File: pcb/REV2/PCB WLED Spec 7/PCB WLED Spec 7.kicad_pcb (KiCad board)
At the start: 2 copper layers, 12 parts, among them J1 USB_C_Receptacle_USB2.0_16P, U1 ESP32-C3, U2 RT9013-33GB, U3 LMR14050SDDAR

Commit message: Update PCB WLED Spec 7.kicad_pcb
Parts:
- added Q1: BC807, Package_TO_SOT_SMD:SOT-23, F.Cu at (163.1, 134.8)
- added Q2: BC807, Package_TO_SOT_SMD:SOT-23, F.Cu at (163.1, 139.5)
- moved D1 19.6 mm to (163.1, 130.2)
- moved U1 17.0 mm to (170.6, 122.0)
- moved U2 8.75 mm to (177.6, 137.6)
- moved C10 3.95 mm to (157.8, 136.2)
- moved C9 3.95 mm to (157.8, 132.8)
- moved J1 3.95 mm to (160.9, 123.2)
- moved C11 3.95 mm to (157.8, 139.5)
- moved C8 3.95 mm to (157.8, 129.5)
- moved S2 3.71 mm to (177.6, 124.4)
- moved S1 3.71 mm to (177.6, 120.3)
- moved U3 1.68 mm to (170.3, 138.5)
- moved D2 1.09 mm to (171.0, 131.2)
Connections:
- net Net-(U1-GPIO2) renamed LED1_IN
- U1 pad 16: unconnected-(U1-GPIO10-Pad16) -> LED2_IN

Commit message: pcb v2 update
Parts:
- removed Q2: BC807, Package_TO_SOT_SMD:SOT-23
- added AE1: 2450AT18A100E, 2450AT18A100E:ANTC3216X140N, F.Cu at (143.8, 96.2)
- added C1: C1µF, Capacitor_SMD:C_0402_1005Metric, F.Cu at (160.9, 95.9)
- added C12: C0.1µF, Capacitor_SMD:C_0402_1005Metric, F.Cu at (197.0, 82.5)
- added C13: C22nF, Capacitor_SMD:C_0402_1005Metric, F.Cu at (199.5, 86.0)
- added C14: C0.1µF, Capacitor_SMD:C_0402_1005Metric, F.Cu at (189.5, 83.0)
- added C15: C4.7µF, Capacitor_SMD:C_0805_2012Metric, F.Cu at (189.0, 86.5)
- added C16: C4.7µF, Capacitor_SMD:C_0805_2012Metric, F.Cu at (189.0, 84.5)
- added C2: C1µF, Capacitor_SMD:C_0402_1005Metric, F.Cu at (160.9, 97.9)
- added C3: C1µF, Capacitor_SMD:C_0402_1005Metric, F.Cu at (160.9, 99.9)
- added C4: C1µF, Capacitor_SMD:C_0402_1005Metric, F.Cu at (163.8, 95.9)
- added C5: C0.1µF, Capacitor_SMD:C_0402_1005Metric, F.Cu at (163.8, 97.9)
- added C6: C10µF, Capacitor_SMD:C_0603_1608Metric, F.Cu at (156.6, 99.0)
- added C7: C0.1µF, Capacitor_SMD:C_0402_1005Metric, F.Cu at (163.8, 99.9)
- added L1: L2nH, Inductor_SMD:L_0603_1608Metric, F.Cu at (156.6, 101.5)
- added L2: L10µH, custom:TECHFUSE SL1050-100M, F.Cu at (204.0, 76.5)
- added R1: R5.1K, Resistor_SMD:R_0402_1005Metric, F.Cu at (188.5, 78.0)
- added R10: R17.8k, Resistor_SMD:R_0402_1005Metric, F.Cu at (197.0, 89.5)
- added R11: R84.5k, Resistor_SMD:R_0402_1005Metric, F.Cu at (192.0, 89.5)
- added R12: R1k, Resistor_SMD:R_0402_1005Metric, F.Cu at (153.2, 88.0)
- added R13: R1k, Resistor_SMD:R_0402_1005Metric, F.Cu at (153.2, 90.0)
- added R2: R5.1K, Resistor_SMD:R_0402_1005Metric, F.Cu at (188.0, 82.0)
- added R3: R22, Resistor_SMD:R_0402_1005Metric_Pad0.72x0.64mm_HandSolder, F.Cu at (189.0, 79.5)
- added R4: R22, Resistor_SMD:R_0402_1005Metric_Pad0.72x0.64mm_HandSolder, F.Cu at (189.0, 80.5)
- added R5: R10k, Resistor_SMD:R_0402_1005Metric, F.Cu at (150.2, 86.0)
- added R6: R10k, Resistor_SMD:R_0402_1005Metric, F.Cu at (150.2, 88.0)
- added R7: R10k, Resistor_SMD:R_0402_1005Metric, F.Cu at (150.2, 90.0)
- added R8: R10k, Resistor_SMD:R_0402_1005Metric, F.Cu at (150.2, 92.0)
- added R9: R100k, Resistor_SMD:R_0402_1005Metric, F.Cu at (199.5, 88.5)
- added S3: solder pad, custom:solder pad small, F.Cu at (189.5, 89.0)
- added S4: solder pad, custom:solder pad small, F.Cu at (187.5, 89.0)
- added S5: solder pad, custom:solder pad small, F.Cu at (186.0, 71.0)
- added S6: solder pad, custom:solder pad small, F.Cu at (186.0, 73.0)
- added S7: solder pad, custom:solder pad small, F.Cu at (183.5, 71.0)
- added S8: solder pad, custom:solder pad small, F.Cu at (183.5, 73.0)
- moved C11 73.9 mm to (189.0, 72.5), turned to -90 degrees
- moved C10 72.0 mm to (191.5, 72.5), turned to -90 degrees
- moved C9 70.4 mm to (194.0, 72.5), turned to -90 degrees
- moved C8 68.9 mm to (196.5, 72.5), turned to -90 degrees
- moved U2 63.2 mm to (195.7, 77.1)
- moved D1 60.4 mm to (191.6, 77.0)
- moved U3 58.0 mm to (194.8, 86.0)
- moved D2 56.1 mm to (205.0, 86.5)
- moved J1 48.7 mm to (182.9, 79.8), turned to -90 degrees
- moved S2 47.4 mm to (195.5, 80.5)
- moved U1 40.9 mm to (144.0, 90.8)
- moved Q1 39.8 mm to (157.1, 95.5)
- moved S1 32.8 mm to (183.0, 88.0)
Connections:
- U1 pad 16: LED2_IN -> LED1_IN
- U1 pad 6: LED1_IN -> PWM1
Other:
- board outline added: 30 x 20 mm

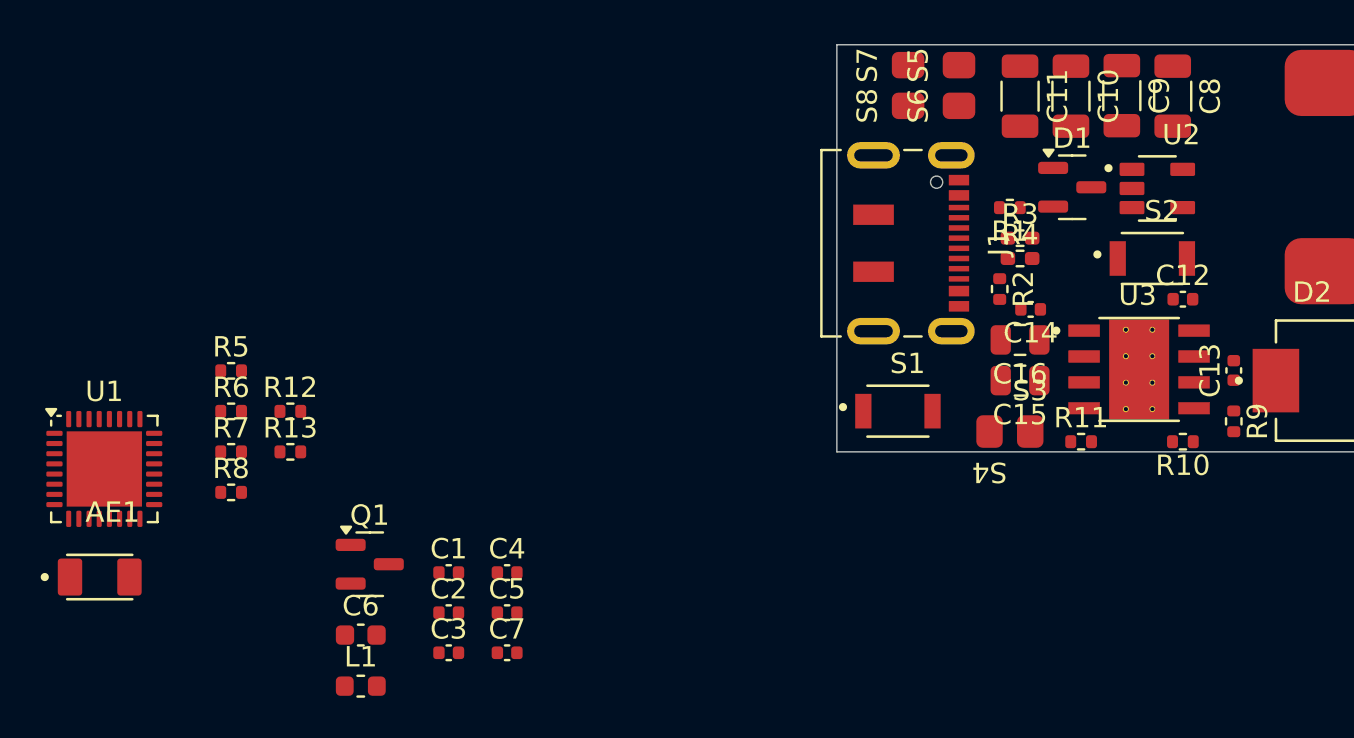
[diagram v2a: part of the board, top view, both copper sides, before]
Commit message: pcb layout finished
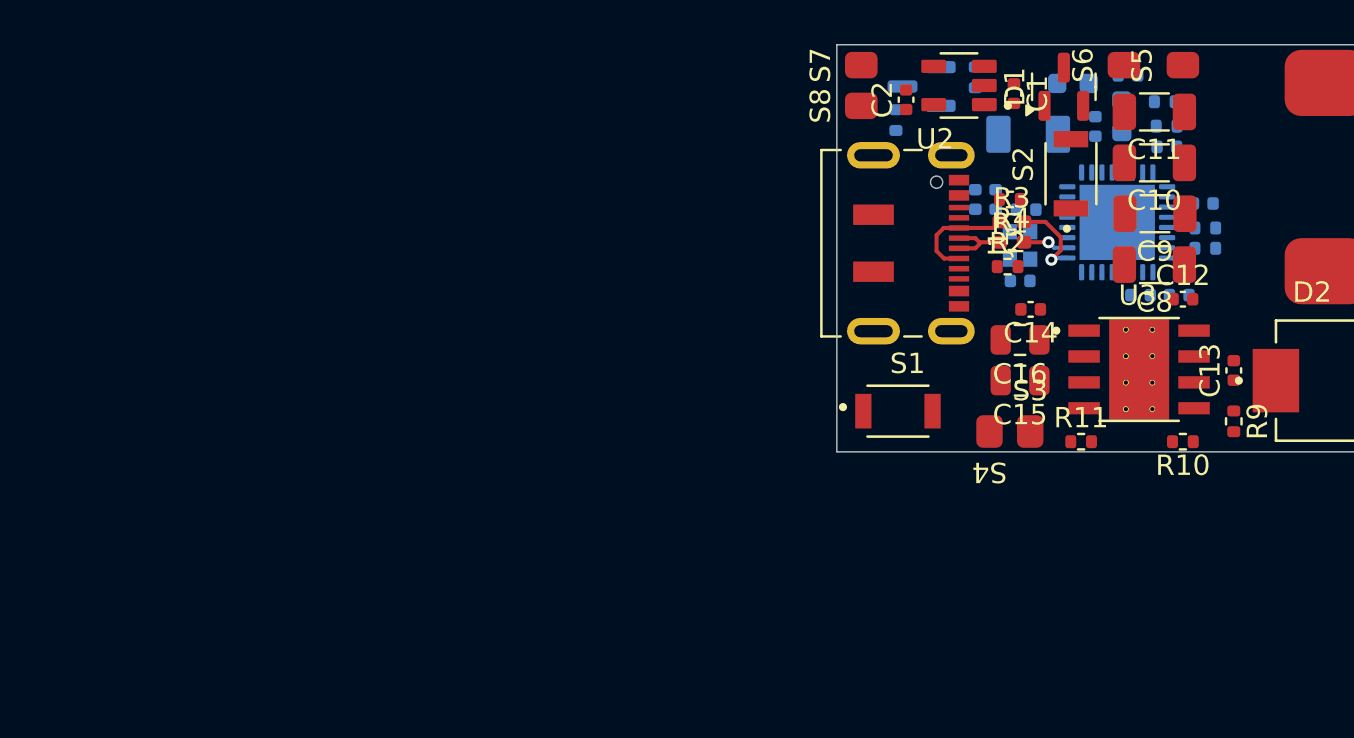
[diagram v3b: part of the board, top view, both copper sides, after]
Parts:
- added C17: C1µF, Capacitor_SMD:C_0402_1005Metric, B.Cu at (194.9, 82.3)
- added C18: C0.1µF, Capacitor_SMD:C_0402_1005Metric, B.Cu at (196.8, 82.3)
- added C19: C1µF, Capacitor_SMD:C_0402_1005Metric, B.Cu at (186.8, 77.6)
- added C20: C10nF, Capacitor_SMD:C_0402_1005Metric, B.Cu at (187.8, 77.6)
- added C21: C12pF, Capacitor_SMD:C_0402_1005Metric, B.Cu at (189.0, 81.6)
- added C22: C12pF, Capacitor_SMD:C_0402_1005Metric, B.Cu at (189.3, 78.1)
- added Y1: XRCGB40M000F1S1DR0, XRCGB40M000F1S1DR0:OSC_XRCGB40M000F1S1DR0, B.Cu at (189.0, 79.9)
- AE1, C3, C4, C5, C6, C7, L1, Q1, R12, R13, R5, R6, R7, R8, U1: moved to B.Cu
- moved U1 51.2 mm to (193.8, 78.7), turned to -90 degrees
- moved AE1 50.5 mm to (189.4, 74.4), turned to 180 degrees
- moved R8 49.4 mm to (196.2, 74.0), turned to 180 degrees
- moved R7 48.9 mm to (198.1, 80.0), turned to 180 degrees
- moved R6 48.7 mm to (198.1, 79.0)
- moved R5 47.7 mm to (196.1, 72.8)
- moved L1 46.7 mm to (194.0, 73.5), turned to 90 degrees
- moved C6 44.3 mm to (191.6, 71.9), turned to 180 degrees
- moved C3 43.2 mm to (196.2, 75.0)
- moved C7 40.7 mm to (198.0, 77.8)
- moved C5 40.3 mm to (194.3, 71.5)
- moved R12 37.4 mm to (186.8, 71.6), turned to 90 degrees
- moved C1 36.4 mm to (188.7, 72.4), turned to -90 degrees
- moved C4 36.3 mm to (192.7, 74.0), turned to 90 degrees
- moved Q1 35.9 mm to (184.2, 72.0), turned to 180 degrees
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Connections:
- U1 pad 17: VDD3P3_CPU -> 3.3V
- U1 pad 31: VDDA -> 3.3V
- U1 pad 32: VDDA -> 3.3V
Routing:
- net Net-(J1-D--PadA7): track 0.00 -> 5.41 mm
- net USB_D-: track 0.00 -> 4.23 mm, vias 0 -> 1
- net Net-(J1-D+-PadA6): track 0.00 -> 3.27 mm
- net USB_D+: track 0.00 -> 2.24 mm, vias 0 -> 1

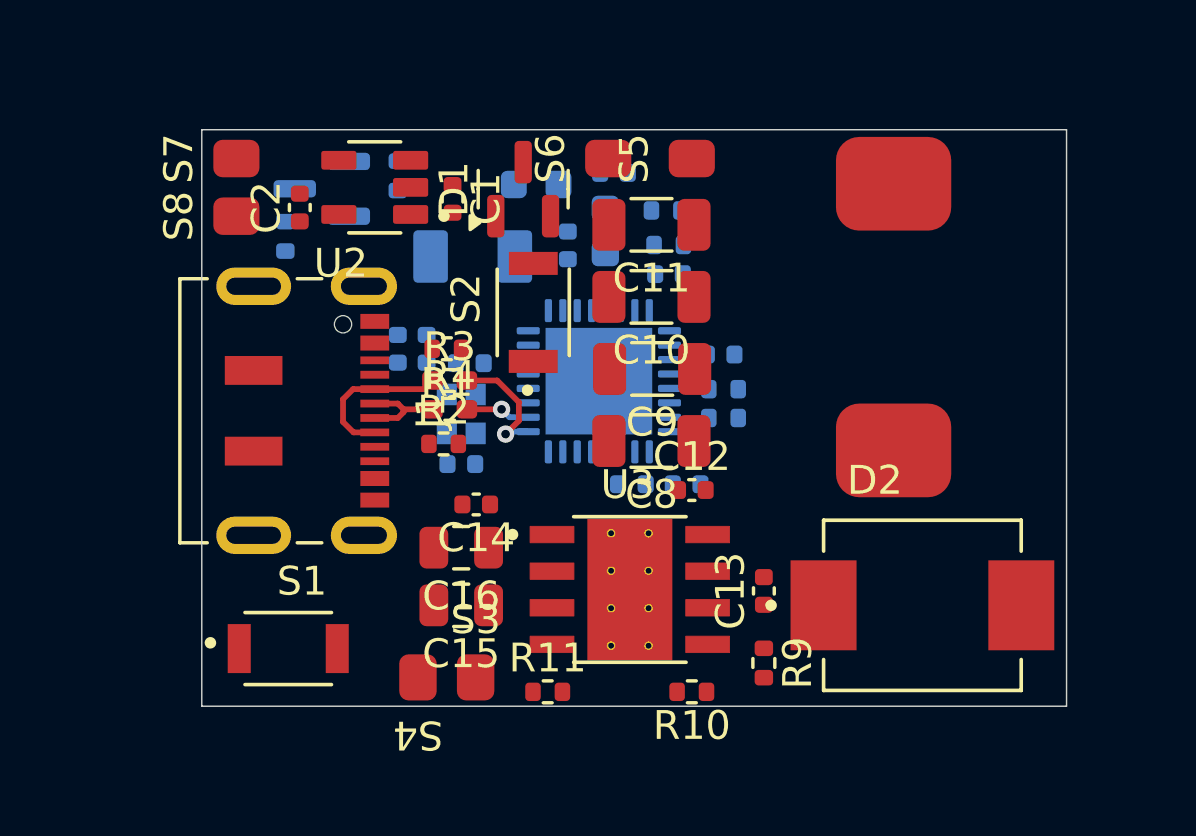
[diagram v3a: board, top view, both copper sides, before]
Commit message: pcb routing done
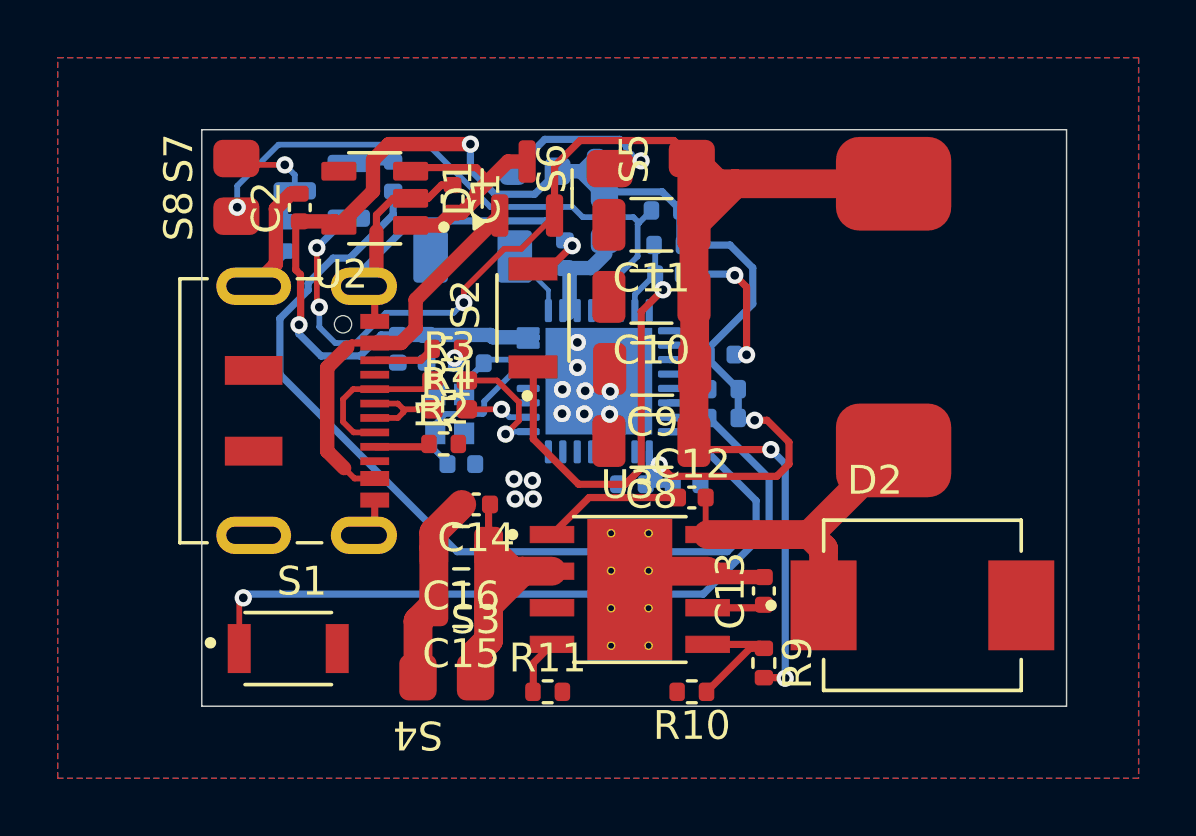
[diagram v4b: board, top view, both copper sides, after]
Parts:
- moved C6 0.46 mm to (191.6, 71.4)
- moved L1 0.46 mm to (194.0, 73.1)
- moved C5 0.46 mm to (194.3, 71.0)
- moved Y1 0.40 mm to (188.6, 79.9)
- moved U2 0.38 mm to (186.0, 72.4)
- moved S6 0.35 mm to (194.2, 71.3)
- moved C4 0.32 mm to (192.6, 74.3)
- moved C12 0.26 mm to (197.0, 82.8)
- moved S2 0.19 mm to (191.5, 76.5)
- moved R12 0.16 mm to (186.6, 71.6)
- moved D1 0.14 mm to (191.3, 72.0)
- moved Q1 0.07 mm to (184.2, 72.1)
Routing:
- net 3.3V: track 0.00 -> 54.0 mm, vias 0 -> 4
- net 5V_BUCK: track 0.00 -> 52.9 mm, vias 0 -> 5
- net GND: track 0.00 -> 49.0 mm, vias 0 -> 17
- net LED1_IN: track 0.00 -> 32.6 mm
- net BOOT: track 0.00 -> 27.1 mm, vias 0 -> 1
- net PWM1: track 0.00 -> 20.6 mm, vias 0 -> 1
- net ENABLE: track 0.00 -> 17.1 mm, vias 0 -> 1
- net 5V_USB: track 0.00 -> 13.7 mm
- net Net-(D2-K): track 0.00 -> 11.6 mm
- net +BATT: track 0.00 -> 10.4 mm
- net 4.5V: track 0.00 -> 8.02 mm
- net XTAL_N: track 0.00 -> 5.76 mm
- net Net-(U3-BOOT): track 0.00 -> 4.90 mm
- net FB: track 0.00 -> 4.62 mm
- net LED1_OUT: track 0.00 -> 4.02 mm, vias 0 -> 1
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- added copper zone on B.Cu, net GND
- added copper zone on F.Cu, net GND

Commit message: pcb afgewerkt
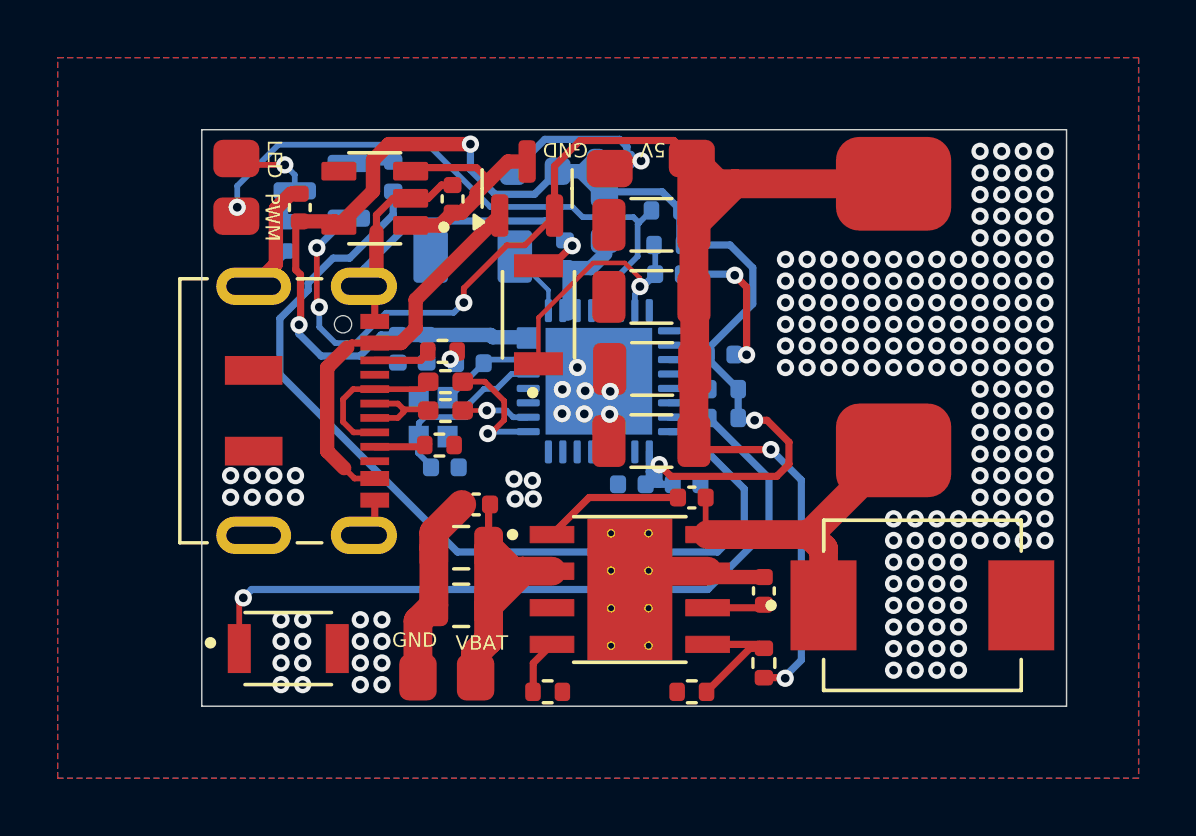
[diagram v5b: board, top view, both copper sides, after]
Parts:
- added G***: LOGO, LOGO, B.Cu at (195.9, 86.6)
- moved C21 0.58 mm to (188.4, 81.7)
- moved Y1 0.58 mm to (188.0, 80.0)
- moved S2 0.22 mm to (191.7, 76.4)
- moved R1 0.18 mm to (188.3, 77.7)
- moved R2 0.15 mm to (188.2, 80.9)
- moved R3 0.15 mm to (188.5, 78.7)
- moved R4 0.15 mm to (188.5, 79.7)
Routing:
- net ENABLE: track 17.1 -> 9.77 mm
- net XTAL_N: track 5.76 -> 6.44 mm
- net LED1_IN: track 32.6 -> 32.0 mm
- net GND: vias 17 -> 202
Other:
- board text added: "5V"
- board text added: "Design by Tore Ladika"
- board text added: "GND"
- board text added: "LED"
- board text added: "PWM"
- board text added: "SPEC7 LED board"
- board text added: "VBAT"
